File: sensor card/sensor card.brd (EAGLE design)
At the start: 100 x 80 mm, 37 parts, among them J1 MJ-3536N, J2 MJ-3536N, U1 PCA9306, X1 S4B-XH-A, X2 S4B-XH-A

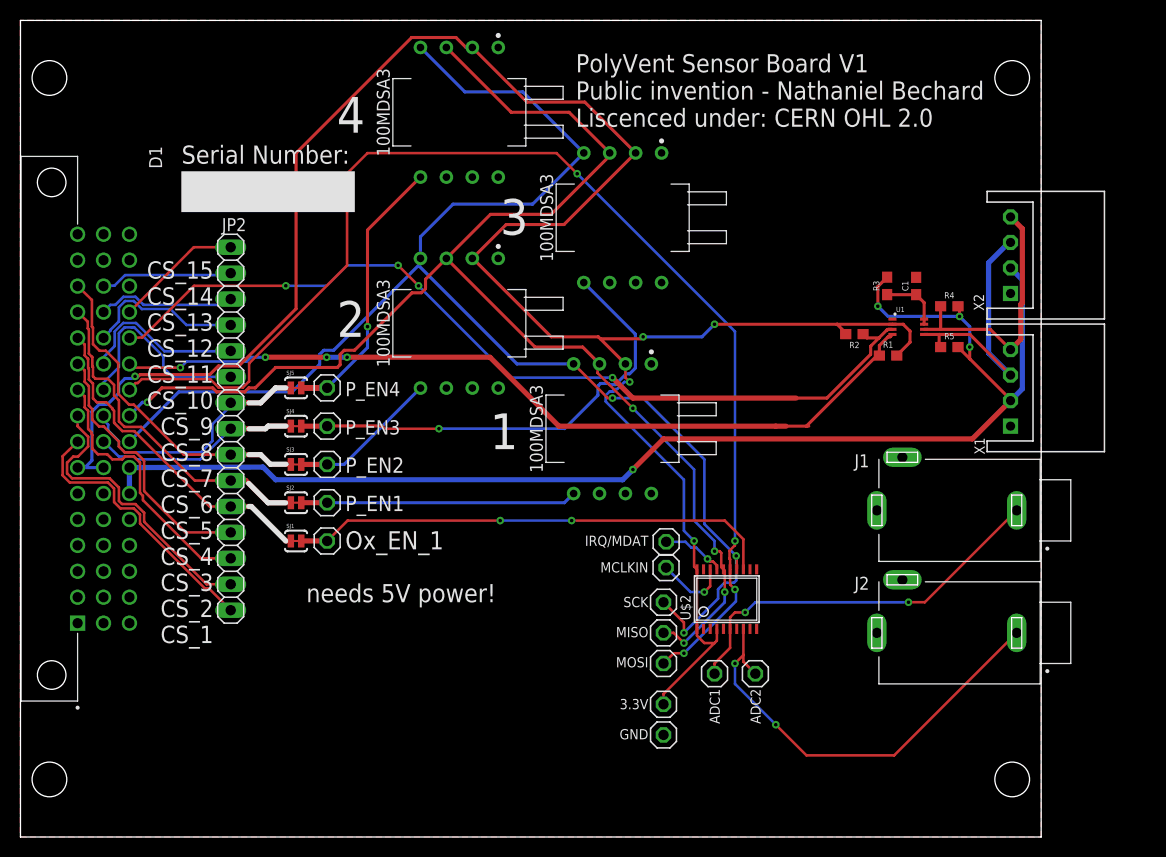
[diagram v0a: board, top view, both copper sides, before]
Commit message: added the new oxygen sensing system to the control module
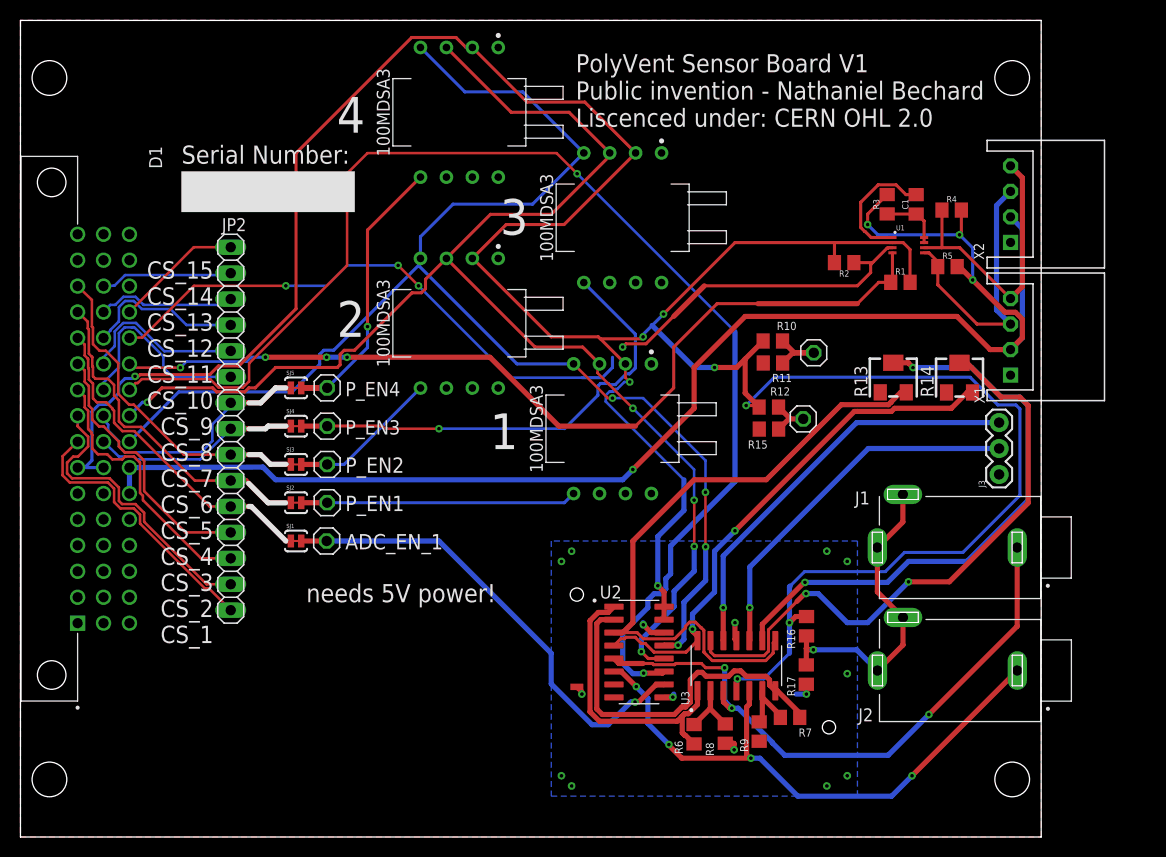
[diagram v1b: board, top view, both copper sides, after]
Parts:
- removed JP1, JP10, JP3, JP4, JP5, JP6, JP7, JP8, JP9: (no value), pinhead:1X01
- added J3: (no value), SparkFun-Connectors:1X03
- added P6, P7: (no value), pinhead:1X01
- added R10: 132k, eagle-ltspice:R0805
- added R11, R8, R9: 1k, eagle-ltspice:R0805
- added R12: 6.5k, eagle-ltspice:R0805
- added R13, R14: (no value), rcl:RTRIM3214W
- added R15: 10k, eagle-ltspice:R0805
- added R16: 16.5k, eagle-ltspice:R0805
- added R17: 100, eagle-ltspice:R0805
- added R6, R7: 30k, eagle-ltspice:R0805
- added U2: MCP3008-I/SL, MCP3008-I_SL:SOIC127P600X175-16N
- added U3: MCP6064-E/SL, MCP6064-E_SL:SOIC127P600X175-14N
- C1: device SparkFun-Capacitors:0603 -> rcl:C0805
- R1, R2, R4, R5: device SparkFun-Resistors:0603 -> eagle-ltspice:R0805
- R3: value 200k -> 200K; device SparkFun-Resistors:0603 -> eagle-ltspice:R0805
- U$2: value MCP346X-E/ST -> EMI_SHIELD; device MCP346XRT-E:ST:TSSOP20 -> emi cap:3671250
- moved P1 51.1 mm to (77.7, 47.4), turned to 180 degrees
- moved U$2 22.6 mm to (54.5, 6.10)
- moved R4 9.42 mm to (91.2, 61.4)
- moved C1 8.00 mm to (87.8, 62.0)
- moved R3 8.00 mm to (84.9, 62.0)
- moved U1 8.00 mm to (87.0, 58.0)
- moved R5 7.88 mm to (90.8, 55.9)
- moved R1 7.27 mm to (86.2, 54.3)
- moved R2 7.07 mm to (80.7, 56.3)
- moved X1 5.00 mm to (97.0, 49.0)
- moved X2 5.00 mm to (97.0, 62.0)
- moved J2 3.69 mm to (92.1, 16.3)
- moved J1 3.64 mm to (92.0, 28.4)
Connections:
- removed net IRQ/MDAT: JP3.1, U$2.17
- removed net MCLKIN: JP1.1, U$2.18
- new net 2V: P7.1, R12.1, R15.2
- new net 50MILIVOLT: P1.1, R10.1, R11.2
- new net AMP_ADC_1: J3.2, U3.10
- new net AMP_ADC_2: J3.3, U3.12
- new net CH0: R6.1, U2.1, U3.1
- new net CH1: R7.1, U2.2, U3.7
- new net CH2: R13.3, U2.3, U3.8
- new net CH3: R14.3, U2.4, U3.14
- new net CH6: U2.7
- new net CH7: U2.8
- new net N$10: R7.2, R9.2, U3.6
- new net N$15: J1.2, J1.3, J2.2, J2.3, R16.1, R17.2
- new net N$2: R14.2, U3.13
- new net N$8: R13.2, U3.9
- new net N$9: R6.2, R8.2, U3.2
- net 3.3V: now also R10.2, R12.2, R16.2, U2.15, U2.16, U3.4; no longer JP9.1, U$2.1, U$2.20, U$2.4
- net GND: now also J3.1, R11.1, R13.1, R14.1, R15.1, R17.1, R8.1, R9.1, U$2.P$1, U2.14, U2.9, U3.11; no longer J1.2, J1.3, J2.2, J2.3, JP10.1, U$2.10, U$2.11, U$2.12, U$2.19, U$2.2, U$2.3, U$2.5, U$2.7, U$2.9
- net MISO: now also U2.12; no longer JP5.1, U$2.16
- net MOSI: now also U2.11; no longer JP6.1, U$2.15
- net N$3: now also P6.1, U2.10; no longer P1.1, U$2.13
- net OXYGEN1: now also U2.5, U3.3; no longer JP8.1, U$2.6
- net OXYGEN2: now also U2.6, U3.5; no longer JP7.1, U$2.8
- net SCK: now also U2.13; no longer JP4.1, U$2.14
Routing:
- net 3.3V: track 210.6 -> 302.7 mm, vias 5 -> 9
- net CH2: track 0.00 -> 64.1 mm
- net N$2: track 0.00 -> 59.4 mm, vias 0 -> 2
- net N$8: track 0.00 -> 57.0 mm, vias 0 -> 2
- net CH3: track 0.00 -> 51.2 mm, vias 0 -> 2
- net AMP_ADC_2: track 0.00 -> 40.7 mm, vias 0 -> 1
- net AMP_ADC_1: track 0.00 -> 36.5 mm, vias 0 -> 1
- net CH1: track 0.00 -> 36.1 mm
- net N$15: track 0.00 -> 31.1 mm, vias 0 -> 1
- net CH0: track 0.00 -> 28.0 mm
- net GND: track 0.33 -> 22.7 mm, vias 0 -> 15
- net OXYGEN1: track 38.6 -> 60.6 mm, vias 2 -> 3
- net 5V: track 131.3 -> 147.7 mm
- net OXYGEN2: track 43.5 -> 58.0 mm, vias 2 -> 4
- net N$9: track 0.00 -> 7.82 mm
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- added copper zone on layer 16, net GND
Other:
- board text added: "ADC_EN_1"
- board text removed: "3.3V GND"
- board text removed: "ADC1 ADC2"
- board text removed: "IRQ/MDAT MCLKIN"
- board text removed: "Ox_EN_1"
- board text removed: "SCK MISO MOSI"

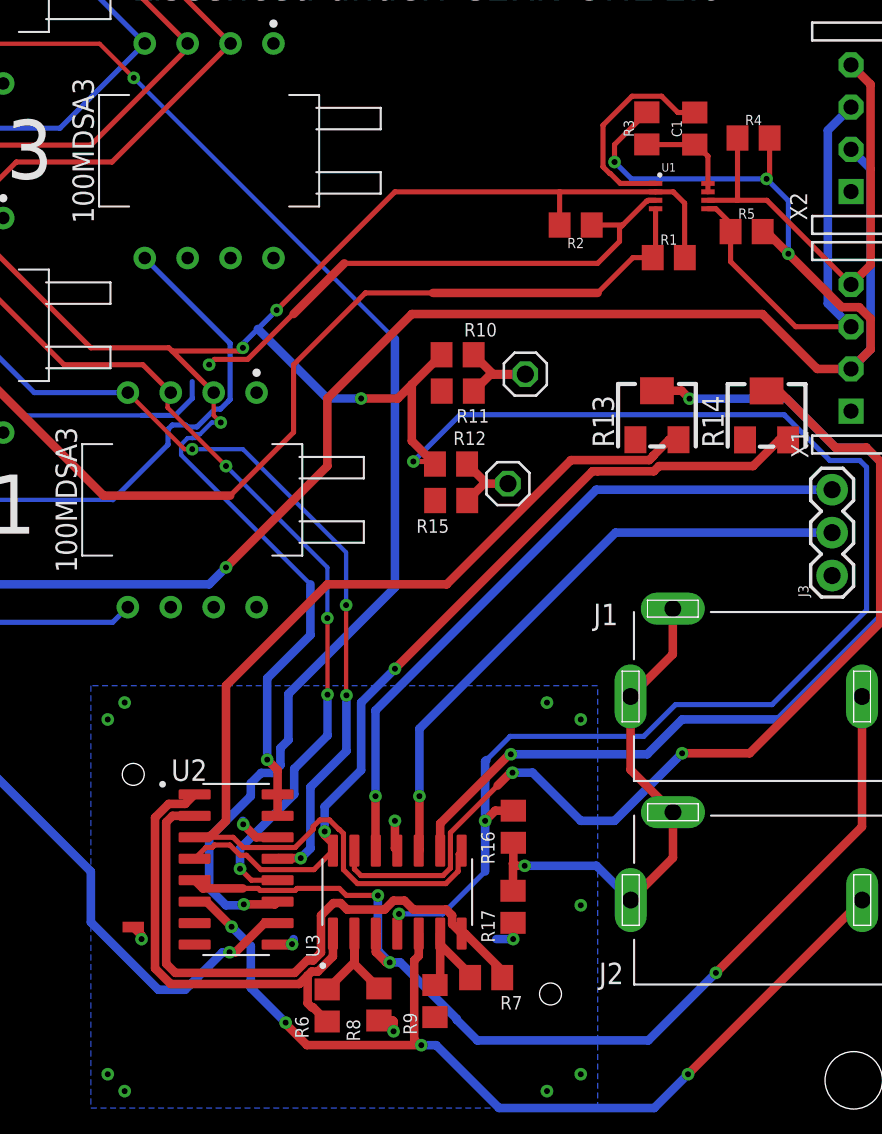
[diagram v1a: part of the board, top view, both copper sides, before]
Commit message: updated libraries to generate better bom's
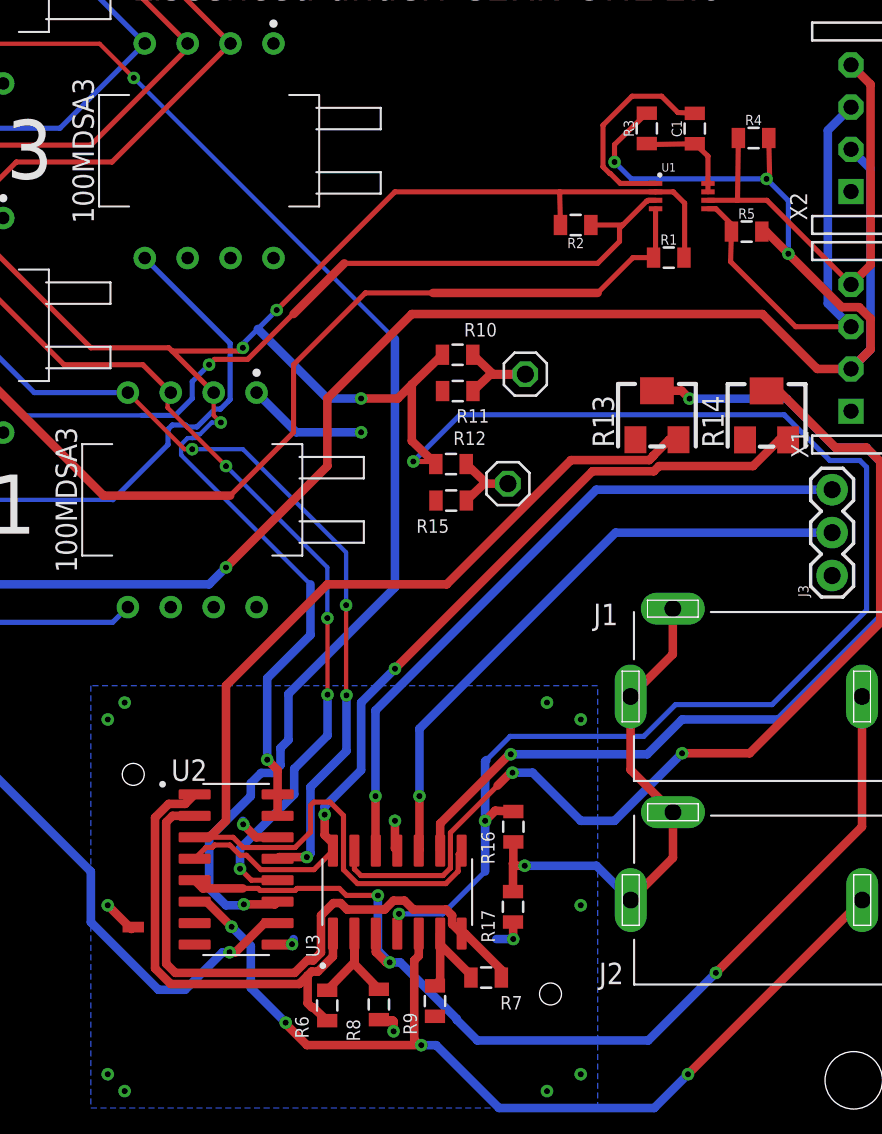
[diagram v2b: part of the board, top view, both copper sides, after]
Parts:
- C1: device rcl:C0805 -> SparkFun-Passives:0805
- R1, R2, R3, R4, R5: device eagle-ltspice:R0805 -> SparkFun-Passives:0805
- R10: value 132k -> 132k, 1%; device eagle-ltspice:R0805 -> SparkFun-Passives:0805
- R11: value 1k -> 1k, 1%; device eagle-ltspice:R0805 -> SparkFun-Passives:0805
- R12: value 6.5k -> 6.5k, 1%; device eagle-ltspice:R0805 -> SparkFun-Passives:0805
- R15: value 10k -> 10k, 1%; device eagle-ltspice:R0805 -> SparkFun-Passives:0805
- R16: value 16.5k -> 16.5k, 1%; device eagle-ltspice:R0805 -> SparkFun-Passives:0805
- R17: value 100 -> 100, 1%; device eagle-ltspice:R0805 -> SparkFun-Passives:0805
- R6, R7: value 30k -> 30k, 0.1%, 25ppm/C; device eagle-ltspice:R0805 -> SparkFun-Passives:0805
- R8, R9: value 1k -> 1k, 0.1%, 25ppm/C; device eagle-ltspice:R0805 -> SparkFun-Passives:0805
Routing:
- net GND: track 22.7 -> 31.2 mm, vias 15 -> 16
- net CH2: track 64.1 -> 66.5 mm
- net SCL: track 89.0 -> 90.4 mm

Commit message: finished V2.2 control module update
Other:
- board text added: "PolyVent Sensor Board V1.1 Public invention - Nathaniel Bechard Liscenced under: CERN OHL 2.0"
- board text added: "needs 5V & 3.3V power!"
- board text removed: "PolyVent Sensor Board V1 Public invention - Nathaniel Bechard Liscenced under: CERN OHL 2.0"
- board text removed: "needs 5V power!"
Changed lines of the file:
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@@
 <grid distance="1" unitdist="mm" unit="mm" style="lines" multiple="1" display="no" altdistance="0.01" altunitdist="mm" altunit="mm"/>
 <layers>
-<layer number="1" name="Top" color="4" fill="1" visible="yes" active="yes"/>
+<layer number="1" name="Top" color="4" fill="1" visible="no" active="yes"/>
 <layer number="2" name="Route2" color="16" fill="1" visible="no" active="no"/>
 <layer number="3" name="Route3" color="17" fill="1" visible="no" active="no"/>
@@
 <layer number="14" name="Route14" color="22" fill="1" visible="no" active="no"/>
 <layer number="15" name="Route15" color="23" fill="1" visible="no" active="no"/>
-<layer number="16" name="Bottom" color="1" fill="1" visible="yes" active="yes"/>
+<layer number="16" name="Bottom" color="1" fill="1" visible="no" active="yes"/>
 <layer number="17" name="Pads" color="2" fill="1" visible="yes" active="yes"/>
 <layer number="18" name="Vias" color="2" fill="1" visible="yes" active="yes"/>
@@
 <text x="31.82" y="39.43" size="1.4" layer="25">P_EN3</text>
 <text x="31.82" y="43.18" size="1.4" layer="25">P_EN4</text>
-<text x="54.41" y="69.58" size="1.778" layer="25">PolyVent Sensor Board V1
+<text x="54.41" y="69.58" size="1.778" layer="25">PolyVent Sensor Board V1.1
 Public invention - Nathaniel Bechard
 Liscenced under: CERN OHL 2.0</text>
-<rectangle x1="22.26" y1="54.72" x2="26.26" y2="71.72" layer="25" rot="R90"/>
-<text x="32.25" y="67.74" size="1.778" layer="25" rot="R180">Serial Number:</text>
-<text x="28" y="23" size="1.778" layer="25">needs 5V power!</text>
+<rectangle x1="34.26" y1="9.72" x2="38.26" y2="26.72" layer="25" rot="R90"/>
+<text x="44.25" y="22.74" size="1.778" layer="25" rot="R180">Serial Number:</text>
+<text x="9.16" y="62.77" size="1.778" layer="25">needs 5V &amp; 3.3V power!</text>
 </plain>
 <attributes>
